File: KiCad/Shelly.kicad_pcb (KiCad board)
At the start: 2 copper layers, 15 x 30 mm, 15 parts, among them J1 Shelly 1, J2 Shelly 2, J3 Shelly i3, J4 USB-C, M1 D24V5F3-NoSHDN, U1 FT231XQ, U2 G3VM-61VY3(TR)

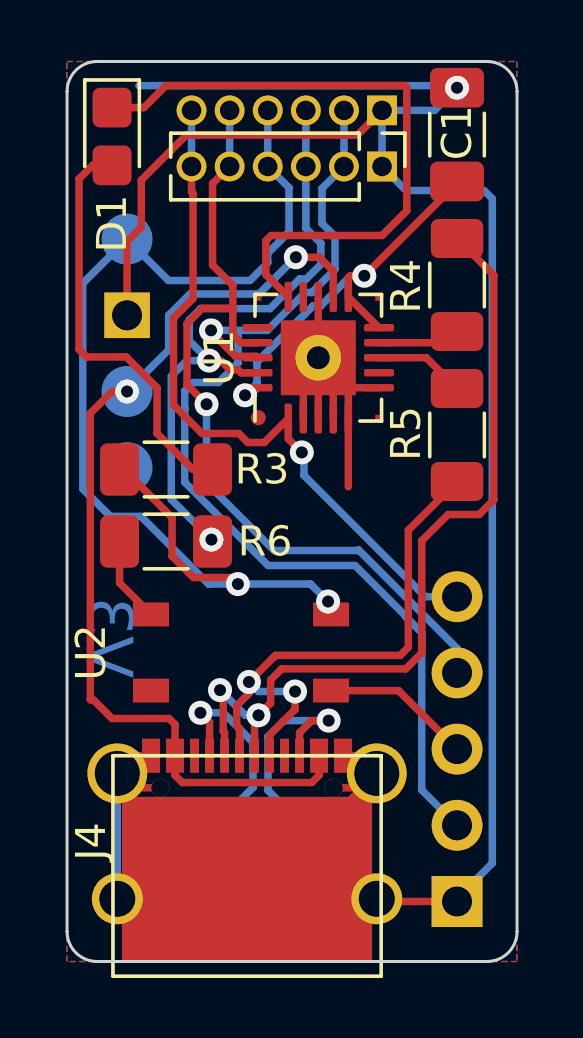
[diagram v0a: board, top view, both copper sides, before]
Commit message: Updated to use new regulator
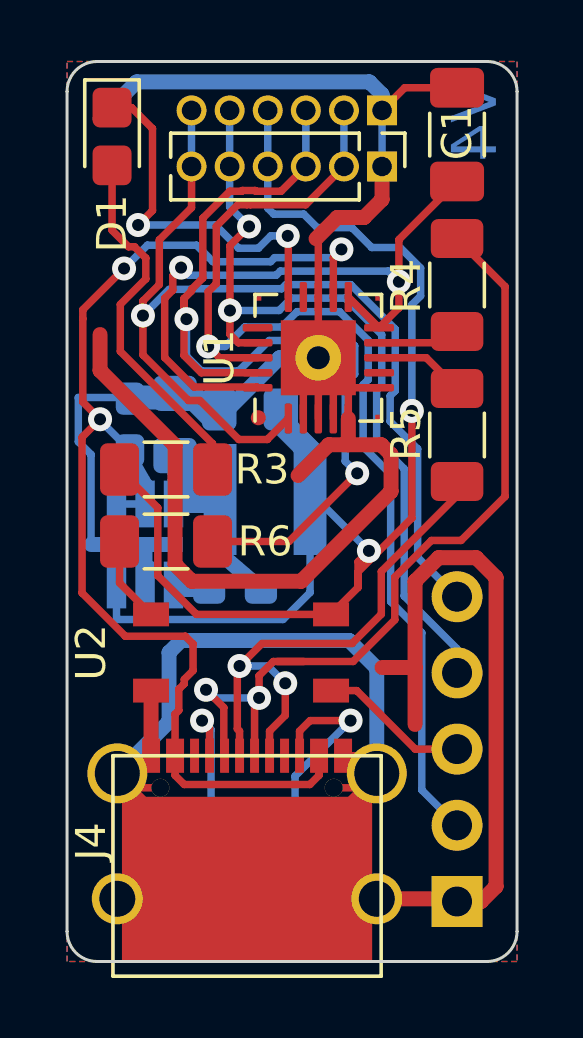
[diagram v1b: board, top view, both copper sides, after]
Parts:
- removed M1: D24V5F3-NoSHDN, RevK:D24V5F3-SMD-Like
- added Reg1: 3.3V, RevK:RegulatorBlock, B.Cu at (172.6, 75.1)
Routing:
- net GND: track 99.2 -> 143.9 mm, vias 1 -> 0
- net RST: track 21.4 -> 32.6 mm
- net TXD: track 23.7 -> 34.5 mm
- net Net-(D1-Pad1): track 21.6 -> 12.6 mm, vias 0 -> 2
- net VBUS: track 32.0 -> 40.7 mm, vias 2 -> 3
- net Net-(C1-Pad1): track 13.6 -> 21.7 mm
- net +3V3: track 36.6 -> 39.8 mm
- net Net-(J4-PadA5): track 7.12 -> 4.83 mm
- net Net-(D1-Pad2): track 14.0 -> 12.3 mm
- net Net-(J4-PadA7): track 28.0 -> 28.7 mm
- net GPIO0: track 35.9 -> 36.6 mm
- net Net-(J4-PadB5): track 7.42 -> 6.86 mm
- net RXD: track 27.7 -> 27.2 mm, vias 1 -> 2
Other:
- board text added: "V4"
- board text removed: "V3"

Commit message: Regulator
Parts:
- C1: footprint Capacitor_SMD:C_1206_3216Metric_Pad1.33x1.80mm_HandSolder -> Capacitor_SMD:C_0603_1608Metric_Pad1.08x0.95mm_HandSolder
- D1: footprint LED_SMD:LED_0805_2012Metric_Castellated -> LED_SMD:LED_0603_1608Metric_Pad1.05x0.95mm_HandSolder
- R1, R2, R3, R4, R5, R6: footprint Resistor_SMD:R_1206_3216Metric_Pad1.30x1.75mm_HandSolder -> Resistor_SMD:R_0603_1608Metric_Pad0.98x0.95mm_HandSolder
- moved C1 3.22 mm to (182.0, 64.5), turned to 0 degrees
- moved R3 1.75 mm to (173.7, 74.3)
- moved R6 0.98 mm to (173.7, 75.9)
- moved R5 0.95 mm to (183.0, 70.5)
- moved R2 0.60 mm to (177.0, 86.0)
- moved R4 0.55 mm to (183.0, 67.0)
- moved R1 0.21 mm to (175.0, 86.0)
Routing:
- net GND: track 143.9 -> 132.8 mm, vias 0 -> 1
- net RST: track 32.6 -> 25.4 mm
- net Net-(C1-Pad1): track 21.7 -> 19.3 mm
- net Net-(D1-Pad2): track 12.3 -> 14.8 mm
- net Net-(J4-PadA7): track 28.7 -> 26.8 mm
- net Net-(J4-PadA6): track 18.4 -> 19.8 mm
- net Net-(R6-Pad1): track 2.86 -> 1.54 mm
- net VBUS: track 40.7 -> 39.6 mm
- net Net-(J4-PadB5): track 6.86 -> 7.81 mm
- net Net-(J4-PadA5): track 4.83 -> 5.61 mm
- net +3V3: track 39.8 -> 40.2 mm, vias 2 -> 3

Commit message: Reg
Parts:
- moved C1 1.41 mm to (183.0, 63.5), turned to 90 degrees
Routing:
- net +3V3: track 40.2 -> 33.6 mm
- net GND: track 132.8 -> 130.3 mm
- net VBUS: track 39.6 -> 37.5 mm
- net Net-(C1-Pad1): track 19.3 -> 21.2 mm

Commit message: Footprint tidy
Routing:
- net GND: track 130.3 -> 117.2 mm
